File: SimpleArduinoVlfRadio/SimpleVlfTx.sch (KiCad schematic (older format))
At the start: 0 parts

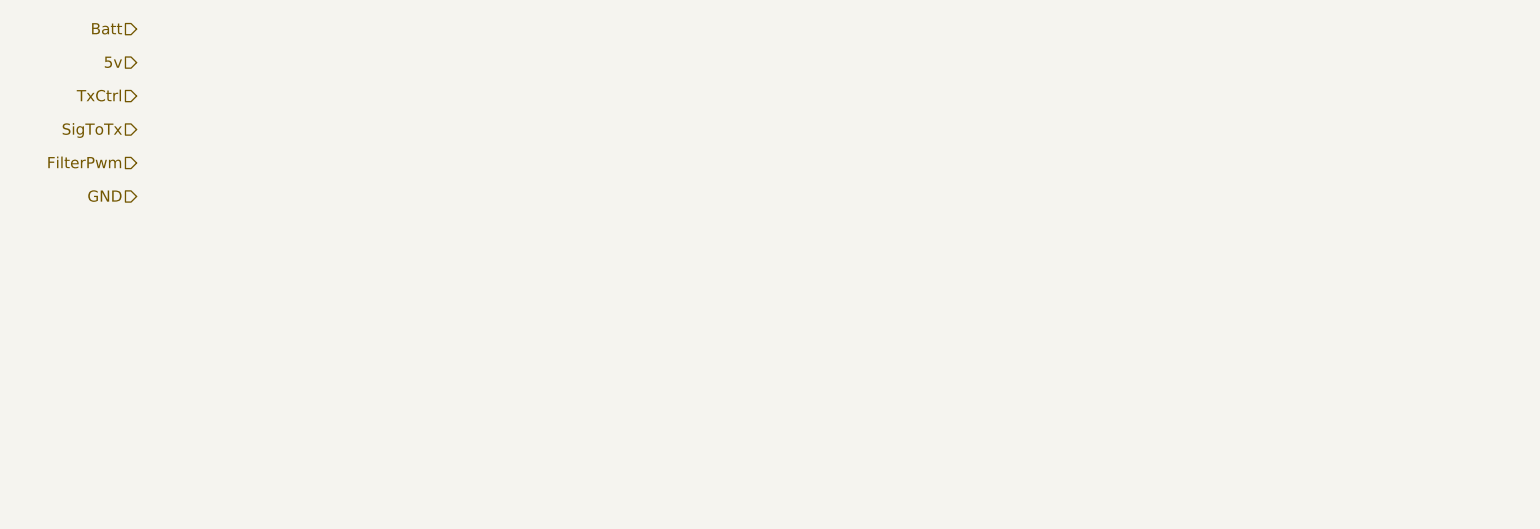
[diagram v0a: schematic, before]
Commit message: Add Transmitter without off switch
Add the main transmitter circuit. Still need to add the ditigal switch to prevent transmitter and receiver from using same antenna.
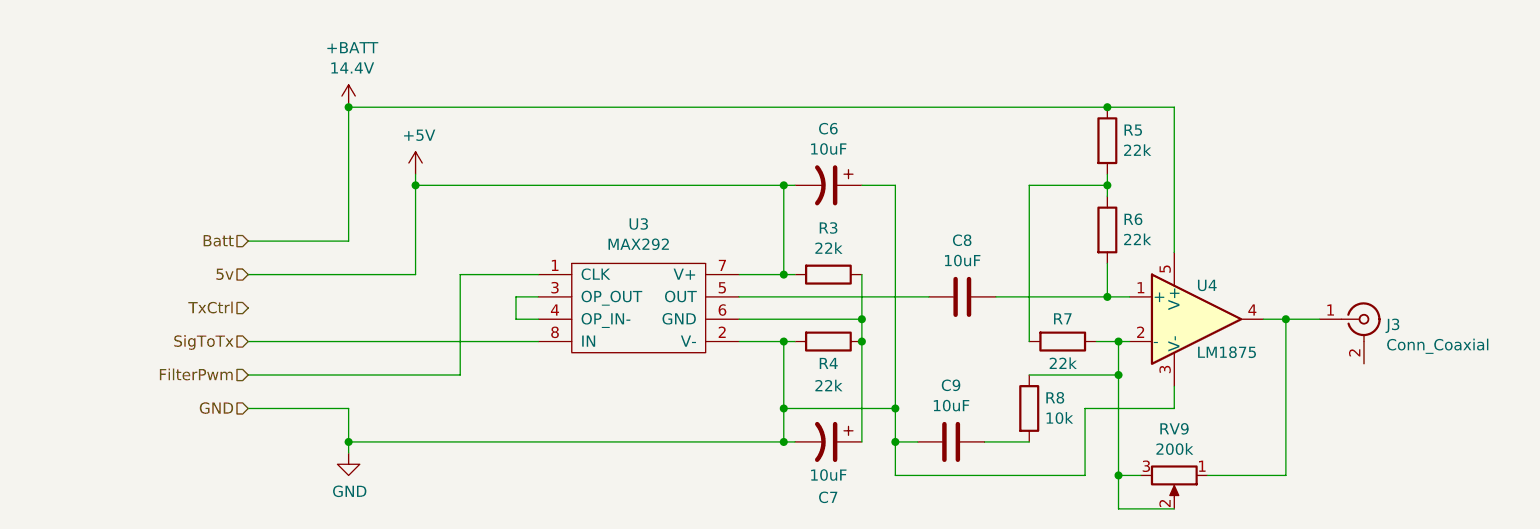
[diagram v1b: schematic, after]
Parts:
- added C6, C7: 10uF, symbol Device:CP1
- added C8, C9: 10uF, symbol Device:C
- added J3: Conn_Coaxial, symbol Connector:Conn_Coaxial
- added R3, R4, R5, R6, R7: 22k, symbol Device:R
- added R8: 10k, symbol Device:R
- added RV9: 200k, symbol Device:R_POT
- added U3: MAX292, Package_DIP:DIP-8_W7.62mm, symbol Custom_Library:MAX292
- added U4: LM1875, Package_TO_SOT_THT:TO-220-5_P3.4x3.7mm_StaggerOdd_Lead3.8mm_Vertical, symbol Amplifier_Audio:LM1875
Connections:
- net FilterPwm: now also U3.1 (CLK)
- net GND: now also C6.1, C7.2, C9.2, R4.2, U3.2 (V-), U4.3 (V-)
- net SigToTx: now also U3.8 (IN)
- new net: U3.3 (OP_OUT), U3.4 (OP_IN-)
- new net: C8.2, U3.5 (OUT)
- new net: C7.1, R3.1, R4.1, U3.6 (GND)
- new net: C8.1, R6.2, U4.1 (+)
- new net: R7.1, R8.1, RV9.2, RV9.3, U4.2 (-)
- new net: J3.1 (In), RV9.1, U4.4
- new net: R5.2, R6.1, R7.2
- new net: C9.1, R8.2
- new net +5V: C6.2, R3.2, U3.7 (V+)
- new net +BATT: R5.1, U4.5 (V+)

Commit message: updates
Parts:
- added R3: 3.3k, symbol Device:R
- added R4, R5: 10k, symbol Device:R
- C6, C7: value 10uF -> 100nF; symbol Device:CP1 -> Device:C
- C8: value 10uF -> 1uF
- C9: symbol Device:C -> Device:CP1
- renumbered R7 to R10, R8 to R11, R3 to R6, R4 to R7, R5 to R8, R6 to R9, RV9 to RV12
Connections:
- net +5V: now also C6.1, R4.1; no longer C6.2
- net GND: now also C6.2, R5.2; no longer C6.1
- net SigToTx: now also R3.2; no longer U3.8 (IN)
- new net: R3.1, R4.2, R5.1, U3.8 (IN)
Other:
- note added: "0.1uF?"
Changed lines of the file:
@@
 $EndComp
-Wire Wire Line
-	1950 2650 3250 2650
 Wire Wire Line
 	1950 2800 2900 2800
@@
 	2900 2350 3250 2350
 Wire Wire Line
-	2400 3100 4350 3100
+	2400 3100 3050 3100
 Connection ~ 2400 3100
 Wire Wire Line
@@
 	2700 1900 2700 1950
 Wire Wire Line
-	2700 1950 4350 1950
+	2700 1950 3050 1950
 Wire Wire Line
 	4350 1950 4350 2350
@@
 	4350 2650 4150 2650
 $Comp
-L Device:R R3
+L Device:R R6
 U 1 1 5EB784CC
 P 4550 2350
-F 0 "R3" V 4343 2350 50  0000 C CNN
+F 0 "R6" V 4343 2350 50  0000 C CNN
 F 1 "22k" V 4434 2350 50  0000 C CNN
 F 2 "" V 4480 2350 50  0001 C CNN
@@
 $EndComp
 $Comp
-L Device:R R4
+L Device:R R7
 U 1 1 5EB78ECC
 P 4550 2650
-F 0 "R4" V 4650 2650 50  0000 C CNN
+F 0 "R7" V 4650 2650 50  0000 C CNN
 F 1 "22k" V 4750 2650 50  0000 C CNN
 F 2 "" V 4480 2650 50  0001 C CNN
@@
 Connection ~ 4350 2650
 $Comp
-L Device:CP1 C6
-U 1 1 5EB7B151
-P 4550 1950
-F 0 "C6" V 4298 1950 50  0000 C CNN
-F 1 "10uF" V 4389 1950 50  0000 C CNN
-F 2 "" H 4550 1950 50  0001 C CNN
-F 3 "~" H 4550 1950 50  0001 C CNN
-	1    4550 1950
-	0    1    1    0
-$EndComp
-$Comp
-L Device:CP1 C7
+L Device:C C7
 U 1 1 5EB7C418
 P 4550 3100
 F 0 "C7" V 4800 3100 50  0000 C CNN
-F 1 "10uF" V 4700 3100 50  0000 C CNN
+F 1 "100nF" V 4700 3100 50  0000 C CNN
 F 2 "" H 4550 3100 50  0001 C CNN
 F 3 "~" H 4550 3100 50  0001 C CNN
@@
 	4700 3100 4700 2650
 Connection ~ 4700 2650
-Wire Wire Line
-	4400 1950 4350 1950
-Connection ~ 4350 1950
 Wire Wire Line
 	4700 1950 4850 1950
@@
 P 5150 2450
 F 0 "C8" V 4898 2450 50  0000 C CNN
-F 1 "10uF" V 4989 2450 50  0000 C CNN
+F 1 "1uF" V 4989 2450 50  0000 C CNN
 F 2 "" H 5188 2300 50  0001 C CNN
 F 3 "~" H 5150 2450 50  0001 C CNN
@@
 $EndComp
 $Comp
-L Device:R R6
+L Device:R R9
 U 1 1 5EB854EC
 P 5800 2150
-F 0 "R6" H 5870 2196 50  0000 L CNN
+F 0 "R9" H 5870 2196 50  0000 L CNN
 F 1 "22k" H 5870 2105 50  0000 L CNN
 F 2 "" V 5730 2150 50  0001 C CNN
@@
 $EndComp
 $Comp
-L Device:R R5
+L Device:R R8
 U 1 1 5EB87026
 P 5800 1750
-F 0 "R5" H 5870 1796 50  0000 L CNN
+F 0 "R8" H 5870 1796 50  0000 L CNN
 F 1 "22k" H 5870 1705 50  0000 L CNN
 F 2 "" V 5730 1750 50  0001 C CNN
@@
 $EndComp
 $Comp
-L Device:C C9
+L Device:CP1 C9
 U 1 1 5EB8C9BB
 P 5100 3100
@@
 $EndComp
 $Comp
-L Device:R_POT RV9
+L Device:R_POT RV12
 U 1 1 5EB8D92D
 P 6100 3250
-F 0 "RV9" V 5893 3250 50  0000 C CNN
+F 0 "RV12" V 5893 3250 50  0000 C CNN
 F 1 "200k" V 5984 3250 50  0000 C CNN
 F 2 "" H 6100 3250 50  0001 C CNN
@@
 Connection ~ 4850 3100
 $Comp
-L Device:R R8
+L Device:R R11
 U 1 1 5EB8BEF7
 P 5450 2950
-F 0 "R8" H 5520 2996 50  0000 L CNN
+F 0 "R11" H 5520 2996 50  0000 L CNN
 F 1 "10k" H 5520 2905 50  0000 L CNN
 F 2 "" V 5380 2950 50  0001 C CNN
@@
 $EndComp
 $Comp
-L Device:R R7
+L Device:R R10
 U 1 1 5EB87631
 P 5600 2650
-F 0 "R7" V 5500 2650 50  0000 C CNN
+F 0 "R10" V 5500 2650 50  0000 C CNN
 F 1 "22k" V 5700 2650 50  0000 C CNN
 F 2 "" V 5530 2650 50  0001 C CNN
@@
 	6600 2550 6750 2550
 Connection ~ 6600 2550
+$Comp
+L Device:R R3
+U 1 1 5EBB5525
+P 2600 2650
+F 0 "R3" V 2700 2650 50  0000 C CNN
+F 1 "3.3k" V 2484 2650 50  0000 C CNN
+F 2 "" V 2530 2650 50  0001 C CNN
+F 3 "~" H 2600 2650 50  0001 C CNN
+	1    2600 2650
+	0    1    1    0
+$EndComp
+$Comp
+L Device:R R4
+U 1 1 5EBB64FA
+P 3050 2150
+F 0 "R4" H 3120 2196 50  0000 L CNN
+F 1 "10k" H 3120 2105 50  0000 L CNN
+F 2 "" V 2980 2150 50  0001 C CNN
+F 3 "~" H 3050 2150 50  0001 C CNN
+	1    3050 2150
+	1    0    0    -1
+$EndComp
+$Comp
+L Device:R R5
+U 1 1 5EBB6F4F
+P 3050 2900
+F 0 "R5" H 3120 2946 50  0000 L CNN
+F 1 "10k" H 3120 2855 50  0000 L CNN
+F 2 "" V 2980 2900 50  0001 C CNN
+F 3 "~" H 3050 2900 50  0001 C CNN
+	1    3050 2900
+	1    0    0    -1
+$EndComp
+Wire Wire Line
+	1950 2650 2450 2650
+Wire Wire Line
+	2750 2650 3050 2650
+Wire Wire Line
+	3050 2750 3050 2650
+Connection ~ 3050 2650
+Wire Wire Line
+	3050 2650 3250 2650
+Wire Wire Line
+	3050 2650 3050 2300
+Wire Wire Line
+	3050 2000 3050 1950
+Connection ~ 3050 1950
+Wire Wire Line
+	3050 1950 4350 1950
+Wire Wire Line
+	3050 3050 3050 3100
+Connection ~ 3050 3100
+Wire Wire Line
+	3050 3100 4350 3100
+Text Notes 5050 2150 0    50   ~ 0
+0.1uF?
+Connection ~ 4350 1950
+Wire Wire Line
+	4400 1950 4350 1950
+$Comp
+L Device:C C6
+U 1 1 5EB7B151
+P 4550 1950
+F 0 "C6" V 4800 1950 50  0000 C CNN
+F 1 "100nF" V 4700 1950 50  0000 C CNN
+F 2 "" H 4550 1950 50  0001 C CNN
+F 3 "~" H 4550 1950 50  0001 C CNN
+	1    4550 1950
+	0    -1   -1   0
+$EndComp
 $EndSCHEMATC
